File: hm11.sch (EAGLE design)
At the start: 3 parts

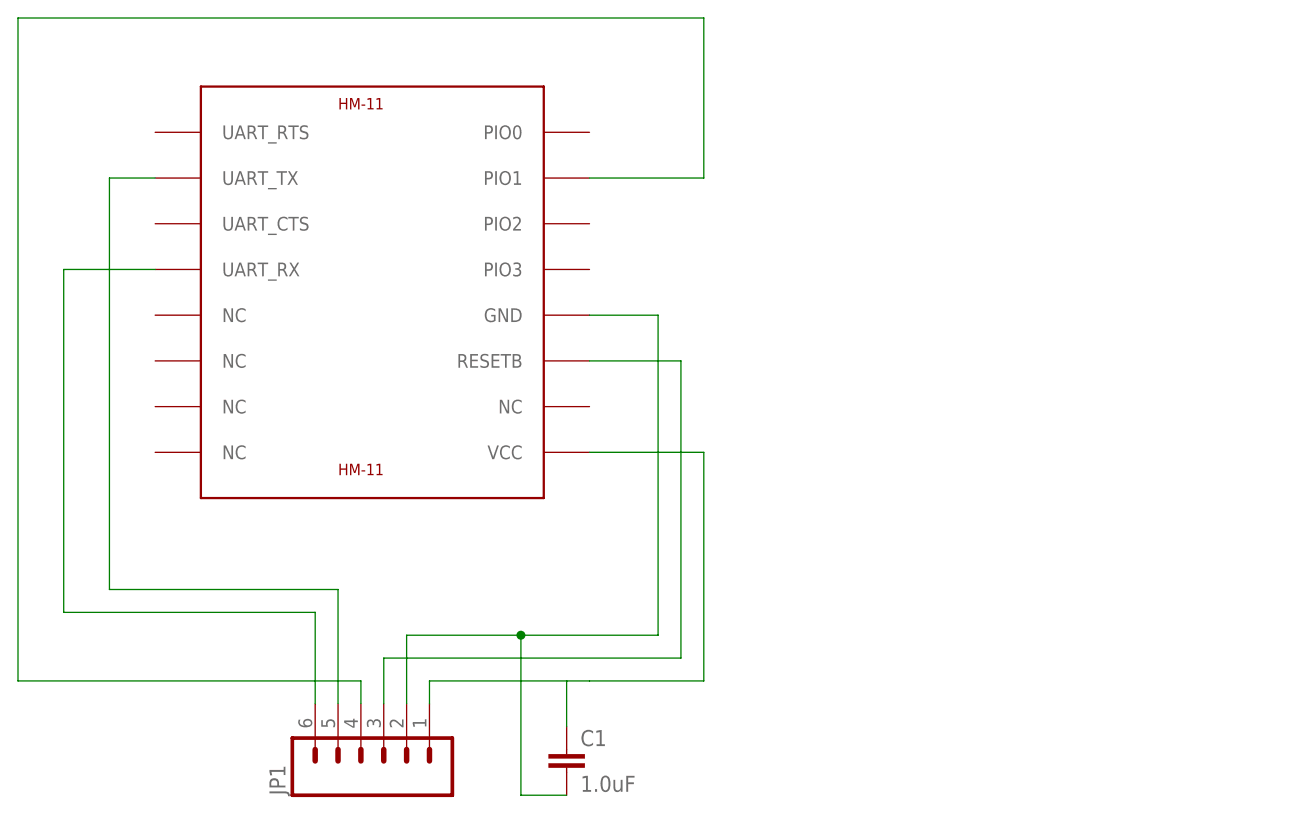
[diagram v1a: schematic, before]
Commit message: Updated pin locations
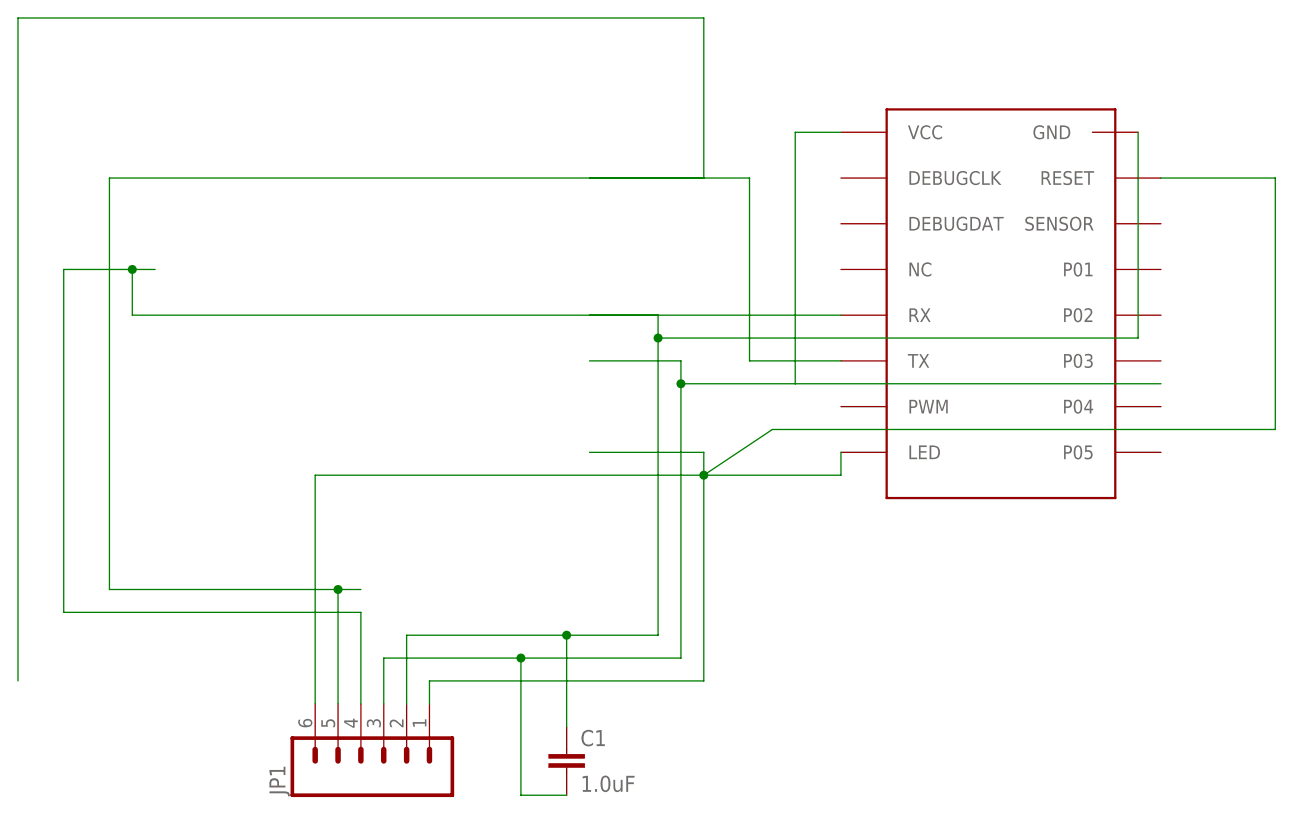
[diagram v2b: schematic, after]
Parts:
- removed U$1: HM-11, hm-11:HM-11
- added U$2: JDR08, hm-11:JDR08
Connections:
- removed net N$4: JP1.4, U$1.PIO1
- removed net N$6: JP1.3, U$1.RESETB
- new net N$7: JP1.6, U$2.LED
- new net N$8: C1.2, JP1.3, U$2.VCC
- net GND: now also C1.1, U$2.GND; no longer C1.2, U$1.GND
- net N$2: now also U$2.RESET; no longer C1.1, U$1.VCC
- net N$3: now also U$2.TX; no longer U$1.UART_TX
- net N$5: now also JP1.4, U$2.RX; no longer JP1.6, U$1.UART_RX
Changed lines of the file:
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@@
 </classes>
 <parts>
-<part name="U$1" library="hm-11" deviceset="HM-11" device=""/>
 <part name="JP1" library="SparkFun-Connectors" deviceset="M06" device="SIP"/>
 <part name="C1" library="SparkFun-Capacitors" deviceset="1.0UF" device="-0603-16V-10%" value="1.0uF"/>
+<part name="U$2" library="hm-11" deviceset="JDR08" device=""/>
 </parts>
 <sheets>
@@
 </plain>
 <instances>
-<instance part="U$1" gate="G$1" x="68.58" y="45.72"/>
 <instance part="JP1" gate="G$1" x="71.12" y="-5.08" rot="R90"/>
 <instance part="C1" gate="G$1" x="91.44" y="-7.62"/>
+<instance part="U$2" gate="G$1" x="137.16" y="45.72"/>
 </instances>
 <busses>
@@
 <net name="N$4" class="0">
 <segment>
-<pinref part="U$1" gate="G$1" pin="PIO1"/>
 <wire x1="93.98" y1="58.42" x2="106.68" y2="58.42" width="0.1524" layer="91"/>
 <wire x1="106.68" y1="58.42" x2="106.68" y2="76.2" width="0.1524" layer="91"/>
 <wire x1="106.68" y1="76.2" x2="30.48" y2="76.2" width="0.1524" layer="91"/>
 <wire x1="30.48" y1="76.2" x2="30.48" y2="2.54" width="0.1524" layer="91"/>
-<wire x1="30.48" y1="2.54" x2="68.58" y2="2.54" width="0.1524" layer="91"/>
-<pinref part="JP1" gate="G$1" pin="4"/>
-<wire x1="68.58" y1="0" x2="68.58" y2="2.54" width="0.1524" layer="91"/>
 </segment>
 </net>
 <net name="N$2" class="0">
 <segment>
-<pinref part="U$1" gate="G$1" pin="VCC"/>
 <wire x1="93.98" y1="27.94" x2="106.68" y2="27.94" width="0.1524" layer="91"/>
-<wire x1="106.68" y1="27.94" x2="106.68" y2="2.54" width="0.1524" layer="91"/>
+<wire x1="106.68" y1="27.94" x2="106.68" y2="25.4" width="0.1524" layer="91"/>
 <pinref part="JP1" gate="G$1" pin="1"/>
-<wire x1="106.68" y1="2.54" x2="93.98" y2="2.54" width="0.1524" layer="91"/>
-<wire x1="91.44" y1="2.54" x2="76.2" y2="2.54" width="0.1524" layer="91"/>
+<wire x1="106.68" y1="25.4" x2="106.68" y2="2.54" width="0.1524" layer="91"/>
+<wire x1="106.68" y1="2.54" x2="76.2" y2="2.54" width="0.1524" layer="91"/>
 <wire x1="76.2" y1="2.54" x2="76.2" y2="0" width="0.1524" layer="91"/>
-<pinref part="C1" gate="G$1" pin="1"/>
-<wire x1="93.98" y1="2.54" x2="91.44" y2="2.54" width="0.1524" layer="91"/>
-<wire x1="91.44" y1="2.54" x2="91.44" y2="-2.54" width="0.1524" layer="91"/>
-</segment>
-</net>
-<net name="N$6" class="0">
-<segment>
-<pinref part="U$1" gate="G$1" pin="RESETB"/>
-<wire x1="93.98" y1="38.1" x2="104.14" y2="38.1" width="0.1524" layer="91"/>
-<wire x1="104.14" y1="38.1" x2="104.14" y2="5.08" width="0.1524" layer="91"/>
-<wire x1="104.14" y1="5.08" x2="71.12" y2="5.08" width="0.1524" layer="91"/>
-<pinref part="JP1" gate="G$1" pin="3"/>
-<wire x1="71.12" y1="0" x2="71.12" y2="5.08" width="0.1524" layer="91"/>
+<wire x1="106.68" y1="25.4" x2="114.3" y2="30.48" width="0.1524" layer="91"/>
+<junction x="106.68" y="25.4"/>
+<wire x1="114.3" y1="30.48" x2="170.18" y2="30.48" width="0.1524" layer="91"/>
+<wire x1="170.18" y1="30.48" x2="170.18" y2="58.42" width="0.1524" layer="91"/>
+<pinref part="U$2" gate="G$1" pin="RESET"/>
+<wire x1="170.18" y1="58.42" x2="157.48" y2="58.42" width="0.1524" layer="91"/>
 </segment>
 </net>
 <net name="GND" class="0">
 <segment>
-<pinref part="U$1" gate="G$1" pin="GND"/>
 <wire x1="93.98" y1="43.18" x2="101.6" y2="43.18" width="0.1524" layer="91"/>
-<wire x1="101.6" y1="43.18" x2="101.6" y2="7.62" width="0.1524" layer="91"/>
-<wire x1="101.6" y1="7.62" x2="86.36" y2="7.62" width="0.1524" layer="91"/>
+<wire x1="101.6" y1="43.18" x2="101.6" y2="40.64" width="0.1524" layer="91"/>
+<wire x1="101.6" y1="40.64" x2="101.6" y2="7.62" width="0.1524" layer="91"/>
+<wire x1="101.6" y1="7.62" x2="91.44" y2="7.62" width="0.1524" layer="91"/>
 <pinref part="JP1" gate="G$1" pin="2"/>
-<wire x1="86.36" y1="7.62" x2="73.66" y2="7.62" width="0.1524" layer="91"/>
+<wire x1="91.44" y1="7.62" x2="73.66" y2="7.62" width="0.1524" layer="91"/>
 <wire x1="73.66" y1="7.62" x2="73.66" y2="0" width="0.1524" layer="91"/>
-<pinref part="C1" gate="G$1" pin="2"/>
-<wire x1="91.44" y1="-10.16" x2="86.36" y2="-10.16" width="0.1524" layer="91"/>
-<wire x1="86.36" y1="-10.16" x2="86.36" y2="7.62" width="0.1524" layer="91"/>
-<junction x="86.36" y="7.62"/>
+<pinref part="U$2" gate="G$1" pin="GND"/>
+<wire x1="101.6" y1="40.64" x2="154.94" y2="40.64" width="0.1524" layer="91"/>
+<wire x1="154.94" y1="40.64" x2="154.94" y2="63.5" width="0.1524" layer="91"/>
+<junction x="101.6" y="40.64"/>
+<pinref part="C1" gate="G$1" pin="1"/>
+<wire x1="91.44" y1="-2.54" x2="91.44" y2="7.62" width="0.1524" layer="91"/>
+<junction x="91.44" y="7.62"/>
 </segment>
 </net>
 <net name="N$3" class="0">
 <segment>
-<pinref part="U$1" gate="G$1" pin="UART_TX"/>
-<wire x1="45.72" y1="58.42" x2="40.64" y2="58.42" width="0.1524" layer="91"/>
 <wire x1="40.64" y1="58.42" x2="40.64" y2="12.7" width="0.1524" layer="91"/>
 <wire x1="40.64" y1="12.7" x2="66.04" y2="12.7" width="0.1524" layer="91"/>
+<wire x1="66.04" y1="12.7" x2="68.58" y2="12.7" width="0.1524" layer="91"/>
+<wire x1="40.64" y1="58.42" x2="111.76" y2="58.42" width="0.1524" layer="91"/>
+<wire x1="111.76" y1="58.42" x2="111.76" y2="38.1" width="0.1524" layer="91"/>
+<pinref part="U$2" gate="G$1" pin="TX"/>
+<wire x1="111.76" y1="38.1" x2="121.92" y2="38.1" width="0.1524" layer="91"/>
 <pinref part="JP1" gate="G$1" pin="5"/>
-<wire x1="66.04" y1="0" x2="66.04" y2="12.7" width="0.1524" layer="91"/>
+<wire x1="66.04" y1="12.7" x2="66.04" y2="0" width="0.1524" layer="91"/>
+<junction x="66.04" y="12.7"/>
 </segment>
 </net>
 <net name="N$5" class="0">
 <segment>
-<pinref part="U$1" gate="G$1" pin="UART_RX"/>
-<wire x1="45.72" y1="48.26" x2="35.56" y2="48.26" width="0.1524" layer="91"/>
+<wire x1="45.72" y1="48.26" x2="43.18" y2="48.26" width="0.1524" layer="91"/>
+<wire x1="43.18" y1="48.26" x2="35.56" y2="48.26" width="0.1524" layer="91"/>
 <wire x1="35.56" y1="48.26" x2="35.56" y2="10.16" width="0.1524" layer="91"/>
-<wire x1="35.56" y1="10.16" x2="63.5" y2="10.16" width="0.1524" layer="91"/>
-<pinref part="JP1" gate="G$1" pin="6"/>
-<wire x1="63.5" y1="0" x2="63.5" y2="10.16" width="0.1524" layer="91"/>
+<wire x1="35.56" y1="10.16" x2="68.58" y2="10.16" width="0.1524" layer="91"/>
+<pinref part="U$2" gate="G$1" pin="RX"/>
+<wire x1="121.92" y1="43.18" x2="43.18" y2="43.18" width="0.1524" layer="91"/>
+<wire x1="43.18" y1="43.18" x2="43.18" y2="48.26" width="0.1524" layer="91"/>
+<junction x="43.18" y="48.26"/>
+<pinref part="JP1" gate="G$1" pin="4"/>
+<wire x1="68.58" y1="10.16" x2="68.58" y2="0" width="0.1524" layer="91"/>
 </segment>
 </net>
+<net name="N$7" class="0">
+<segment>
+<pinref part="U$2" gate="G$1" pin="LED"/>
+<wire x1="121.92" y1="25.4" x2="121.92" y2="27.94" width="0.1524" layer="91"/>
+<wire x1="63.5" y1="25.4" x2="121.92" y2="25.4" width="0.1524" layer="91"/>
+<pinref part="JP1" gate="G$1" pin="6"/>
+<wire x1="63.5" y1="0" x2="63.5" y2="25.4" width="0.1524" layer="91"/>
+</segment>
+</net>
+<net name="N$8" class="0">
+<segment>
+<pinref part="C1" gate="G$1" pin="2"/>
+<wire x1="91.44" y1="-10.16" x2="86.36" y2="-10.16" width="0.1524" layer="91"/>
+<wire x1="93.98" y1="38.1" x2="104.14" y2="38.1" width="0.1524" layer="91"/>
+<wire x1="104.14" y1="38.1" x2="104.14" y2="35.56" width="0.1524" layer="91"/>
+<wire x1="104.14" y1="35.56" x2="104.14" y2="5.08" width="0.1524" layer="91"/>
+<wire x1="104.14" y1="5.08" x2="86.36" y2="5.08" width="0.1524" layer="91"/>
+<pinref part="JP1" gate="G$1" pin="3"/>
+<wire x1="86.36" y1="5.08" x2="71.12" y2="5.08" width="0.1524" layer="91"/>
+<wire x1="71.12" y1="0" x2="71.12" y2="5.08" width="0.1524" layer="91"/>
+<wire x1="104.14" y1="35.56" x2="116.84" y2="35.56" width="0.1524" layer="91"/>
+<junction x="104.14" y="35.56"/>
+<wire x1="116.84" y1="35.56" x2="157.48" y2="35.56" width="0.1524" layer="91"/>
+<wire x1="116.84" y1="35.56" x2="116.84" y2="63.5" width="0.1524" layer="91"/>
+<pinref part="U$2" gate="G$1" pin="VCC"/>
+<wire x1="116.84" y1="63.5" x2="121.92" y2="63.5" width="0.1524" layer="91"/>
+<wire x1="86.36" y1="-10.16" x2="86.36" y2="5.08" width="0.1524" layer="91"/>
+<junction x="86.36" y="5.08"/>
+</segment>
+</net>
